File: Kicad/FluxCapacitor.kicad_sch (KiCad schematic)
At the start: 94 parts, among them J1 Jack-DC, J10 RELAY, J19 Conn_01x03_Socket, J2 TM_1, J20 Conn_01x03_Socket, J21 Conn_01x03_Socket, J22 Conn_01x03_Socket, J23 Conn_01x03_Socket, J3 TM_2, J4 Conn_01x02, J7 TM_1, J8 TM_1, J9 RELAY, K1 G5V-1, M1 Fan_4pin, Q1 2N7000, Q2 IRF4905PBF, Q3 2N7000, Q4 2N7000, SW1 SW_SPDT_321, U1 OKI-78SR-5_1.5-W36-C, U2 ESP32_DEVBOARD

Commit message: Finished schematic
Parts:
- added C20: 10UF, symbol Device:C_Polarized
- added C21, C24: .1uf, symbol Device:C
- added R33: 10K, symbol Device:R
- added R34, R35, R36, R37: 330Ω, symbol Device:R
- added TP15: TP_P23, symbol Connector:TestPoint
- added TP16: TP_P19, symbol Connector:TestPoint
- added TP17: TP_P18, symbol Connector:TestPoint
- added TP18: TP_BTN_A0, symbol Connector:TestPoint
- added TP19: TP_BTN_A1, symbol Connector:TestPoint
- added TP20: TP_BTN_A2, symbol Connector:TestPoint
- added TP21: TP_BTN_A3, symbol Connector:TestPoint
- added TP22: TP_BTN_A4, symbol Connector:TestPoint
- added TP23: TP_BTN_A5, symbol Connector:TestPoint
- added TP24: TP_BTN_A7, symbol Connector:TestPoint
- added TP25: TP_BTN_B7, symbol Connector:TestPoint
- added U6: SMF5.0A-T13, symbol FluxCapacitor:SMF5.0A-T13
- C2: value 0.1 uf -> 0.1UF
- C3: value 47UF -> 100UF
- D6: value LED -> GREEN
- J1: value Jack-DC -> Barrel_Jack; symbol Connector:Jack-DC -> Connector:Barrel_Jack_Switch
- M1: value Fan_4pin -> SYS_FAN; now not fitted
- Q1, Q3: symbol Generic:2N7000 -> FluxCapacitor:2N7000
- Q4: symbol Generic:2N7000 -> FluxCapacitor:2N7000; now not fitted
- R10: value 100K -> 10K
- R31, R32: now not fitted
- TP12: value TP_12V -> TP_RLY_12V
- U2: symbol ESP32_STUFF:ESP32_DEVBOARD -> FluxCapacitor:ESP32_DEVBOARD
- U7: renamed from U_LED_EXPANDER1; value MCP23017_SP -> MCP23017x-x-SP; symbol Interface_Expansion:MCP23017_SP -> Interface_Expansion:MCP23017x-x-SP
- U8: renamed from U_BTN_EXPANDER1; value MCP23017_SP -> MCP23017x-x-SP; symbol Interface_Expansion:MCP23017_SP -> Interface_Expansion:MCP23017x-x-SP
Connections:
- net DB_RELAY_TRIGG_3 is gone; now on net DB_RELAY_TRIG_3: J10.7
- net SUPERCAP_SENSE is gone; now on net FAN_TACHO: U2.3 (SVP)
- net TP_BTN_B0 is gone; now on net M1_PRESET_BTN: U8.1 (GPB0)
- net TP_BTN_B1 is gone; now on net M1_STARTSTOP_BTN: U8.2 (GPB1)
- net TP_BTN_B2 is gone; now on net M2_PRESET_BTN: U8.3 (GPB2)
- net TP_BTN_B3 is gone; now on net M2_STARTSTOP_BTN: U8.4 (GPB3)
- net TP_BTN_B4 is gone; now on net M3_PRESET_BTN: U8.5 (GPB4)
- net TP_BTN_B5 is gone; now on net M3_STARTSTOP_BTN: U8.6 (GPB5)
- net TP_BTN_B6 is gone; now on net M4_PRESET_BTN: U8.7 (GPB6)
- net +3V3: now also R31.1, U8.17 (A2), R33.2; no longer U8.15 (A0)
- net BTN_EXP_INT: now also U8.19 (INTB); no longer U8.20 (INTA)
- net DBG1: now also U7.25 (GPA4); no longer U7.5 (GPB4)
- net DBG2: now also U7.26 (GPA5); no longer U7.6 (GPB5)
- net DBG3: now also U7.27 (GPA6); no longer U7.7 (GPB6)
- net DBG4: now also U7.28 (GPA7); no longer U7.8 (GPB7)
- net FAN_PWM: now also R31.2, R32.2
- net GND: now also M1.1 (-), U8.15 (A0), C20.2, C21.2, C24.1, U6.A (2); no longer U8.17 (A2)
- net I2C_SCL: now also U7.13 (SDA), U8.13 (SDA); no longer U7.12 (SCK), U8.12 (SCK)
- net I2C_SDA: now also U7.12 (SCK), U8.12 (SCK); no longer U7.13 (SDA), U8.13 (SDA)
- net M1_PRESET_BTN: no longer U8.21 (GPA0)
- net M1_PRESET_LED_1: now also U7.2 (GPB1); no longer U7.22 (GPA1)
- net M1_PRESET_LED_2: now also U7.3 (GPB2); no longer U7.23 (GPA2)
- net M1_PWR_LED: now also U7.1 (GPB0); no longer U7.21 (GPA0)
- net M1_STARTSTOP_BTN: no longer U8.22 (GPA1)
- net M2_PRESET_BTN: no longer U8.23 (GPA2)
- net M2_PRESET_LED_1: now also U7.5 (GPB4); no longer U7.25 (GPA4)
- net M2_PRESET_LED_2: now also U7.6 (GPB5); no longer U7.26 (GPA5)
- net M2_PWR_LED: now also U7.4 (GPB3); no longer U7.24 (GPA3)
- net M2_STARTSTOP_BTN: no longer U8.24 (GPA3)
- net M3_PRESET_BTN: no longer U8.25 (GPA4)
- net M3_PRESET_LED_1: now also U7.8 (GPB7); no longer U7.28 (GPA7)
- net M3_PRESET_LED_2: now also U7.21 (GPA0); no longer U7.1 (GPB0)
- net M3_PWR_LED: now also U7.7 (GPB6); no longer U7.27 (GPA6)
- net M3_STARTSTOP_BTN: no longer U8.26 (GPA5)
- net M4_PRESET_BTN: no longer U8.27 (GPA6)
- net M4_PRESET_LED_1: now also U7.23 (GPA2); no longer U7.3 (GPB2)
- net M4_PRESET_LED_2: now also U7.24 (GPA3); no longer U7.4 (GPB3)
- net M4_PWR_LED: now also U7.22 (GPA1); no longer U7.2 (GPB1)
- net M4_STARTSTOP_BTN: now also U8.27 (GPA6); no longer U8.28 (GPA7)
- net RELAY_TRIG_1: now also R34.1; no longer U2.9 (P25)
- net RELAY_TRIG_2: now also R35.1; no longer U2.10 (P26)
- net RELAY_TRIG_4: now also R37.1; no longer U2.12 (P14)
- net RLY_TRIGGER: now also U6.C (1)
- net 12V_PROTECTED: now reaches R17.1
- net 12V_PROTECTED: now also C1.1, C2.1, D1.1, D4.1 (K), J9.1, J9.4, M1.2 (+), Q2.3 (S), R1.1, TP1.1, U1.1 (IN), C20.1, C21.1
- net RLY_12V: now reaches D5.1 (K), D6.1 (K), K1.2, TP12.1
- net RLY_12V: now also C11.1, C12.1, D7.1 (K), J20.2 (Pin_2)
- net 5V_SYS: now reaches C10.1, C9.1, D2.1 (K), D3.1 (K), R8.1, TP5.1
- net 5V_SYS: now also BZ1.1 (+), C19.2, Q4.3 (D), R19.1, U2.19 (5V)
- net DB_12V: now reaches J10.1
- net DB_12V: now also J10.4, J19.2 (Pin_2), J21.2 (Pin_2), J22.2 (Pin_2), J23.2 (Pin_2)
- net 5V_RAW: now reaches R18.1
- net 5V_RAW: now also C3.1, C4.1, D2.2 (A), TP2.1, U1.3 (OUT)
- net at Q1.2 (G), R10.2, R9.2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: now also C24.2
- net at R32.1: now also Q4.2 (G); no longer R31.2
- net at Q4.1 (S): now also M1.4 (PWM)
- net FAN_TACHO: now reaches M1.3 (Tacho)
- net FAN_TACHO: now also R33.1
- net RELAY_TRIGG_3: no longer names the net of U2.11 (P27)
- net RELAY_TRIGG_3: now also R36.2; no longer J9.7
- net TP_BTN_B7: no longer names the net of U8.8 (GPB7)
- net TP_BTN_B7: now also TP25.1
- net TP_P18: no longer names the net of U2.28 (P18)
- net TP_P18: now also TP17.1
- net TP_P19: no longer names the net of U2.27 (P19)
- net TP_P19: now also TP16.1
- net TP_P23: no longer names the net of U2.21 (P23)
- net TP_P23: now also TP15.1
- new net: TP18.1, U8.21 (GPA0)
- new net: R34.2, U2.9 (P25)
- new net: TP24.1, U8.28 (GPA7)
- new net: R35.2, U2.10 (P26)
- new net: TP20.1, U8.23 (GPA2)
- new net: TP21.1, U8.24 (GPA3)
- new net: R37.2, U2.12 (P14)
- new net: TP22.1, U8.25 (GPA4)
- new net: TP19.1, U8.22 (GPA1)
- new net: TP23.1, U8.26 (GPA5)
- new net RELAY_TRIG_3: J9.7, R36.1
- no-connect marks 23 -> 25
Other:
- note added: "(A7&B7 ARE OUTPUT ONLY)"
- note added: "(MAX ALLOWABLE FAN CURRENT = 100MA)"
- note added: "FAN HEADER"
- note added: "SUPERCAP"
- note removed: "(MAX FAN CURRENT = 100MA)"
- note removed: "OPTIONAL FAN HEADER"
- note removed: "SUPERCAP HOLD UP"
- moved on the sheet: R10, R29, R3, R30, R6, R9, TP12

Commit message: Touchups
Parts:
- C10, C12, C19, C21, C24: value .1uf -> 0.1UF
- C11, C20: symbol Device:C_Polarized -> Device:C
- C4, C5, C6, C7: value 0.1 uf -> 0.1UF
- C8: value 100UF -> 1.5f
- R8: value 33 -> 33Ω
- renumbered U8 to U_BTN_EXPANDER, U7 to U_LED_EXPANDER1
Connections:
- no-connect marks 25 -> 24
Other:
- note added: "12C GPIO EXPANDERS"
- note removed: "12C COMPONENTS"
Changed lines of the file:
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@@
 		)
 	)
-	(text "12C COMPONENTS"
+	(text "12C GPIO EXPANDERS\n"
 		(exclude_from_sim no)
-		(at 23.622 66.04 0)
+		(at 25.908 66.04 0)
 		(effects
 			(font
@@
 	)
 	(no_connect
-		(at 58.42 35.56)
-	)
-	(no_connect
 		(at 125.73 69.85)
 	)
@@
 			)
 		)
-		(property "Value" ".1uf"
-			(at 243.078 151.384 0)
+		(property "Value" "0.1UF"
+			(at 243.84 152.146 0)
 			(show_name no)
 			(do_not_autoplace no)
@@
 			)
 		)
-		(property "Value" "0.1 uf"
+		(property "Value" "0.1UF"
 			(at 36.322 130.302 90)
 			(show_name no)
@@
 			)
 		)
-		(property "Value" ".1uf"
-			(at 258.318 85.344 0)
+		(property "Value" "0.1UF"
+			(at 259.08 86.106 0)
 			(show_name no)
 			(do_not_autoplace no)
@@
 			)
 		)
-		(property "Value" ".1uf"
+		(property "Value" "0.1UF"
 			(at 152.908 95.25 0)
 			(show_name no)
@@
 	)
 	(symbol
-		(lib_id "Device:C_Polarized")
+		(lib_id "Device:C")
 		(at 88.9 113.03 0)
 		(unit 1)
@@
 			)
 		)
-		(property "Description" "Polarized capacitor"
+		(property "Description" "Unpolarized capacitor"
 			(at 88.9 113.03 0)
 			(hide yes)
@@
 		(dnp no)
 		(property "Reference" "R2"
-			(at 59.69 48.768 0)
+			(at 64.77 50.8 90)
 			(show_name no)
 			(do_not_autoplace no)
@@
 		)
 		(property "Value" "27k"
-			(at 59.69 51.308 0)
+			(at 67.056 51.308 90)
 			(show_name no)
 			(do_not_autoplace no)
@@
 		(dnp no)
 		(fields_autoplaced yes)
-		(property "Reference" "U7"
+		(property "Reference" "U_LED_EXPANDER1"
 			(at 45.3233 73.66 0)
 			(show_name no)
@@
 			(project "FluxCapacitor"
 				(path "/feb6d8df-599a-4f82-8f89-f7a3c96de191"
-					(reference "U7")
+					(reference "U_LED_EXPANDER1")
 					(unit 1)
 				)
@@
 			)
 		)
-		(property "Value" "0.1 uf"
+		(property "Value" "0.1UF"
 			(at 34.798 70.358 90)
 			(show_name no)
@@
 			)
 		)
-		(property "Value" ".1uf"
+		(property "Value" "0.1UF"
 			(at 97.028 115.57 0)
 			(show_name no)
@@
 	)
 	(symbol
+		(lib_name "C_Polarized_1")
 		(lib_id "Device:C_Polarized")
 		(at 128.27 97.79 270)
@@
 			)
 		)
-		(property "Value" "100UF"
+		(property "Value" "1.5f"
 			(at 125.73 101.854 90)
 			(show_name no)
@@
 	)
 	(symbol
-		(lib_id "Device:C_Polarized")
+		(lib_id "Device:C")
 		(at 241.3 83.82 180)
 		(unit 1)
@@
 		(dnp no)
 		(property "Reference" "C11"
-			(at 245.872 81.534 0)
+			(at 245.872 81.28 0)
 			(show_name no)
 			(do_not_autoplace no)
@@
 			)
 		)
-		(property "Description" "Polarized capacitor"
+		(property "Description" "Unpolarized capacitor"
 			(at 241.3 83.82 0)
 			(hide yes)
@@
 			)
 		)
-		(property "Value" ".1uf"
+		(property "Value" "0.1UF"
 			(at 94.488 73.914 0)
 			(show_name no)
@@
 		(dnp no)
 		(fields_autoplaced yes)
-		(property "Reference" "U8"
+		(property "Reference" "U_BTN_EXPANDER"
 			(at 45.3233 134.62 0)
 			(show_name no)
@@
 			(project "FluxCapacitor"
 				(path "/feb6d8df-599a-4f82-8f89-f7a3c96de191"
-					(reference "U8")
+					(reference "U_BTN_EXPANDER")
 					(unit 1)
 				)
@@
 			)
 		)
-		(property "Value" "0.1 uf"
+		(property "Value" "0.1UF"
 			(at 72.898 52.578 90)
 			(show_name no)
@@
 			)
 		)
-		(property "Value" "0.1 uf"
+		(property "Value" "0.1UF"
 			(at 93.98 37.084 90)
 			(show_name no)
@@
 		)
 		(property "Value" "SMF5.0A-T13"
-			(at 232.918 97.79 0)
+			(at 241.046 95.504 0)
 			(show_name no)
 			(do_not_autoplace no)
@@
 		(in_pos_files yes)
 		(dnp no)
-		(fields_autoplaced yes)
 		(property "Reference" "R1"
-			(at 67.31 34.2899 0)
+			(at 64.77 36.576 90)
 			(show_name no)
 			(do_not_autoplace no)
@@
 		)
 		(property "Value" "100k"
-			(at 67.31 36.8299 0)
+			(at 67.056 37.592 90)
 			(show_name no)
 			(do_not_autoplace no)
@@
 		(dnp no)
 		(property "Reference" "R8"
-			(at 133.096 90.678 0)
+			(at 132.08 93.726 90)
 			(show_name no)
 			(do_not_autoplace no)
@@
 			)
 		)
-		(property "Value" "33"
-			(at 133.096 92.456 0)
+		(property "Value" "33Ω"
+			(at 134.112 93.98 90)
 			(show_name no)
 			(do_not_autoplace no)

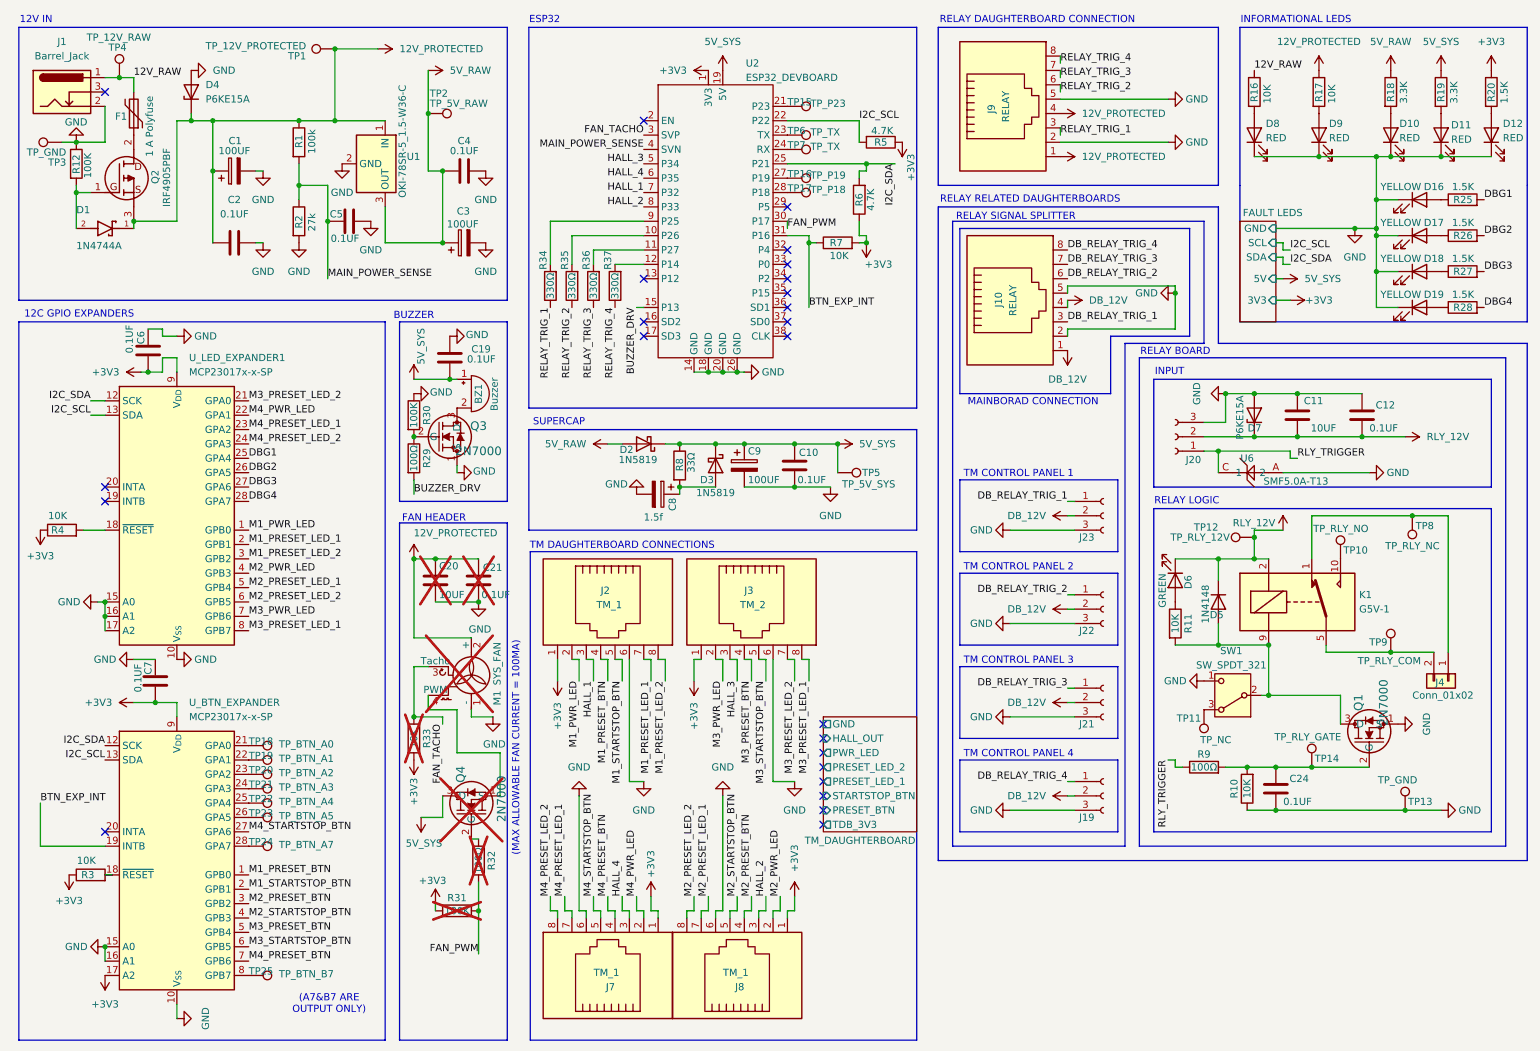
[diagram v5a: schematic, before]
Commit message: Solder jumpers and resistor changes
-Added solder jumpers to seperate power lines during bringup
-changed 10k resistor to 680Ω for the relay board led, to make it much brighter
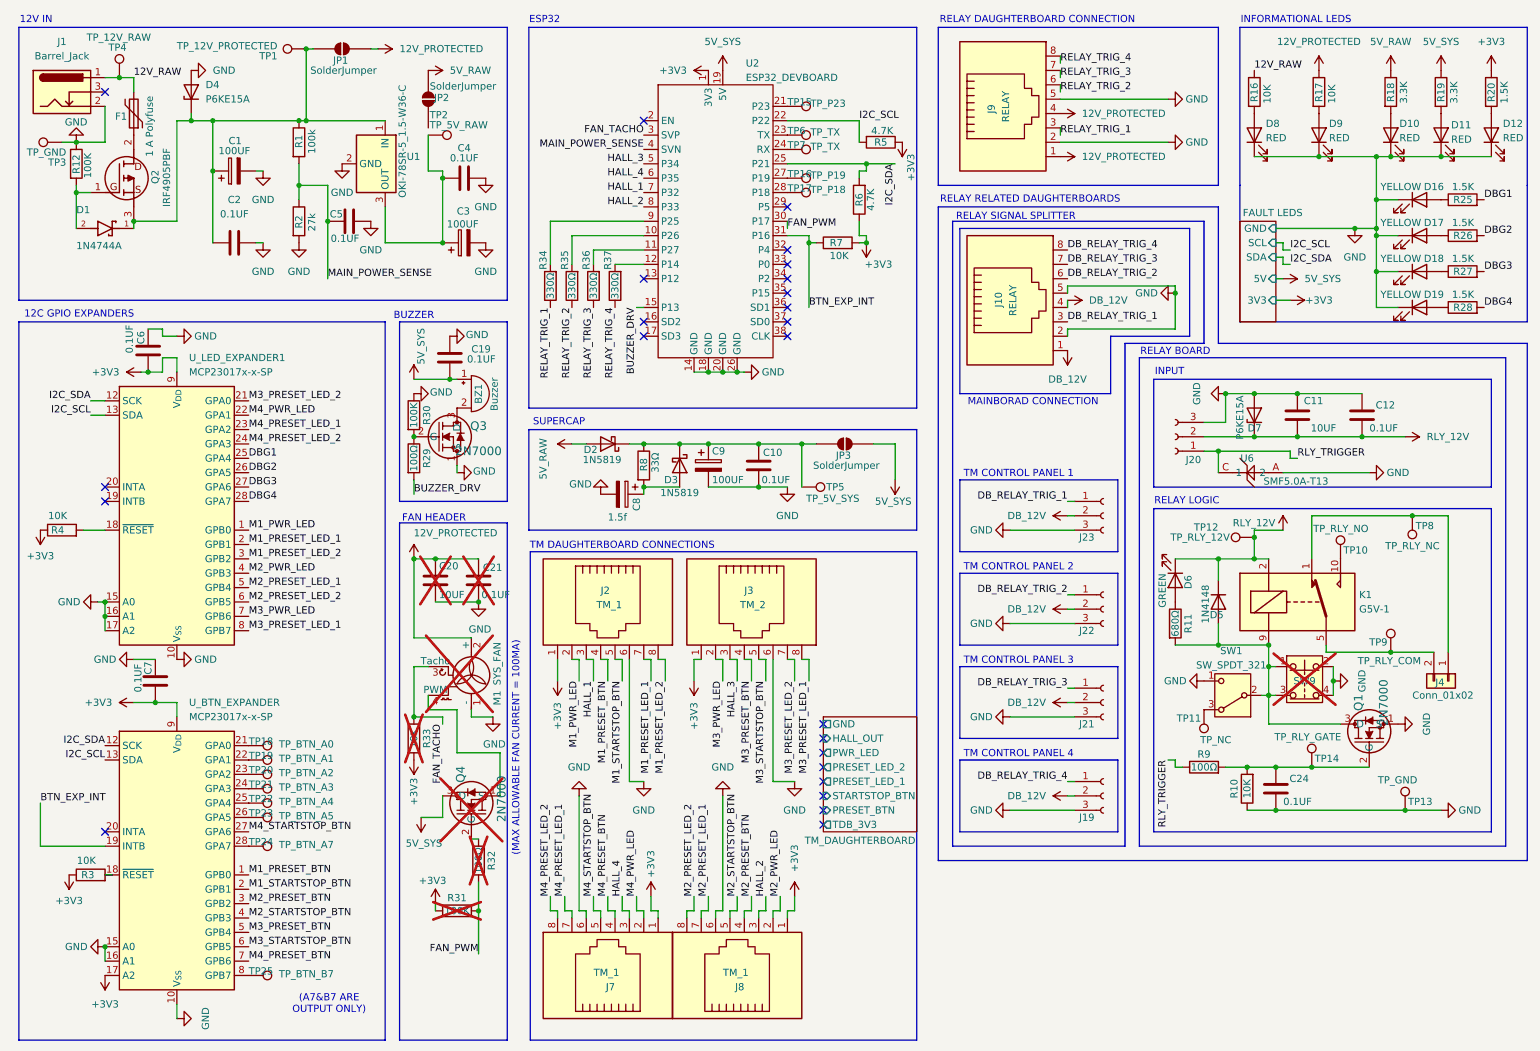
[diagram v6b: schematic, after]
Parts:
- added JP1, JP2, JP3: SolderJumper, symbol Jumper:SolderJumper_2_Open
- added SW9: SW_Push_Open_Dual, symbol Switch:SW_Push_Open_Dual
- R11: value 10K -> 680Ω
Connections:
- net 12V_PROTECTED: now also JP1.2 (B); no longer C1.1, C2.1, D1.1, D4.1 (K), Q2.3 (S), R1.1, TP1.1, U1.1 (IN)
- net 5V_RAW: now also JP2.2 (B); no longer C3.1, C4.1, TP2.1, U1.3 (OUT)
- net 5V_SYS: now also JP3.2 (B); no longer C10.1, C9.1, D2.1 (K), D3.1 (K), R8.1, TP5.1
- net GND: now also SW9.2, SW9.4
- net at D5.2 (A), K1.9, Q1.3 (D)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: now also SW9.1, SW9.3
- new net: C10.1, C9.1, D2.1 (K), D3.1 (K), JP3.1 (A), R8.1, TP5.1
- new net: C1.1, C2.1, D1.1, D4.1 (K), JP1.1 (A), Q2.3 (S), R1.1, TP1.1, U1.1 (IN)
- new net: C3.1, C4.1, TP2.1, U1.3 (OUT)
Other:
- moved on the sheet: C10, C4, C8, C9, D2, D3, R8, TP1, TP2, TP5

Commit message: DNP the TM switch
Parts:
- SW1: now not fitted
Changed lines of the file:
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@@
 		(on_board yes)
 		(in_pos_files yes)
-		(dnp no)
+		(dnp yes)
 		(property "Reference" "SW1"
 			(at 229.616 125.476 0)
@@
 		(dnp no)
 		(property "Reference" "Q1"
-			(at 252.095 134.62 0)
+			(at 259.334 144.018 90)
 			(show_name no)
 			(do_not_autoplace no)
@@
 		)
 		(property "Value" "2N7000"
-			(at 256.54 134.62 0)
-			(show_name no)
-			(do_not_autoplace no)
+			(at 262.382 141.732 90)
+			(show_name no)
+			(do_not_autoplace no)
